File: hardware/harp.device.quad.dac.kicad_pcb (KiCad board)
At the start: 4 copper layers, 90 x 100 mm, 290 parts, among them J1 5-146281-3, J10 Conn_Coaxial, J11 Conn_Coaxial, J12 Conn_Coaxial, J13 Conn_Coaxial, J14 Barrel_Jack_Switch, J15 Conn_Coaxial, J16 Conn_Coaxial, J17 Conn_Coaxial, J18 Conn_Coaxial, J2 5-146281-3, J3 AudioJack3, J4 USB_C_Receptacle_USB2.0, J5 Micro_SD_Card_Det_Hirose_DM3AT, J6 Conn_Coaxial, J7 Conn_Coaxial, J8 Conn_Coaxial, J9 Conn_Coaxial, Q1 Si2369DS, Q2 Si2369DS, Q3 Si2369DS, SW2 SPST-NO, U1 LM337_SOT223, U10 LTC2642, U11 LTC2642, U12 REF3525, U13 LMV393IDGKR, U14 LMV393IDGKR, U15 LMV393IDGKR, U16 LMV393IDGKR, U17 INA630, U18 INA630, U19 INA630, U2 W25Q16JVUXIQ, U20 INA630, U21 REF2033, U22 SN74LVC2T45DCTR, U23 SN74LVC2T45DCTR, U24 rt6150b-33gqw, U25 TPS65131RGE, U27 LM2940IMPX-12/NOPB, U29 LMR51430, U3 ADUM4160, U30 SN74LVC2T45DCTR, U31 SN74LVC2T45DCTR, U32 RP2350_80QFN, U4 OPA2994IDGKR, U5 OPA2994IDGKR, U6 OPA2994IDGKR, U7 OPA2994IDGKR, U8 LTC2642, U9 LTC2642

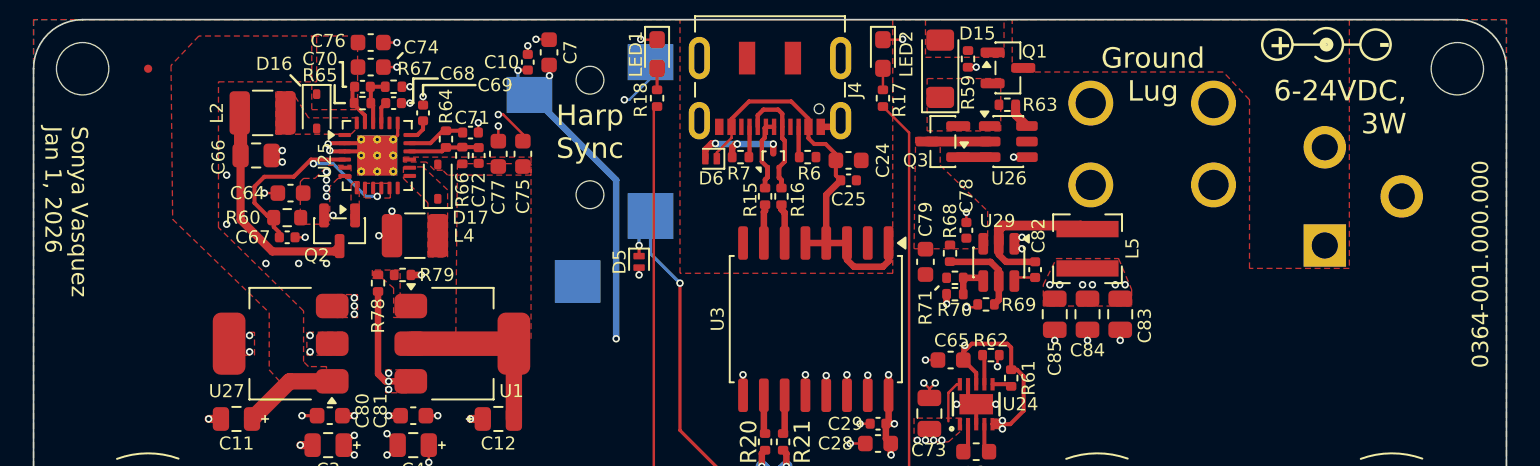
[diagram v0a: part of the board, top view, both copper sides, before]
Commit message: update 1K, 31K6, 10K resistors to 0.1%
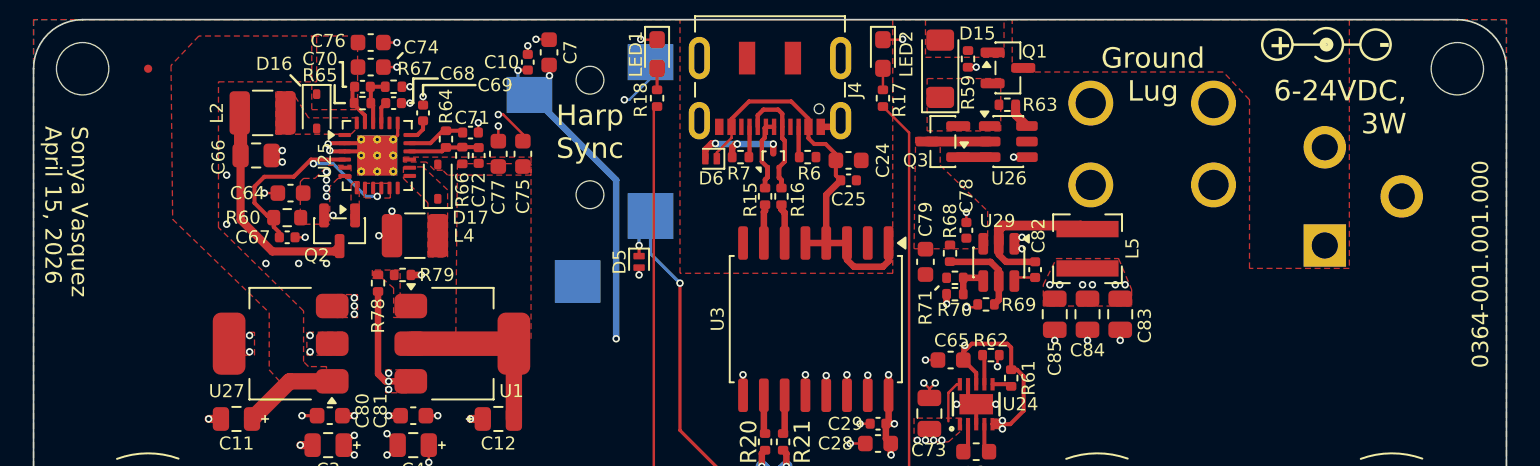
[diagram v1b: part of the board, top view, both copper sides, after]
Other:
- board text added: "0364-001.001.000"
- board text added: "Sonya Vasquez April 15, 2026"
- board text removed: "0364-001.000.000"
- board text removed: "Sonya Vasquez Jan 1, 2026"

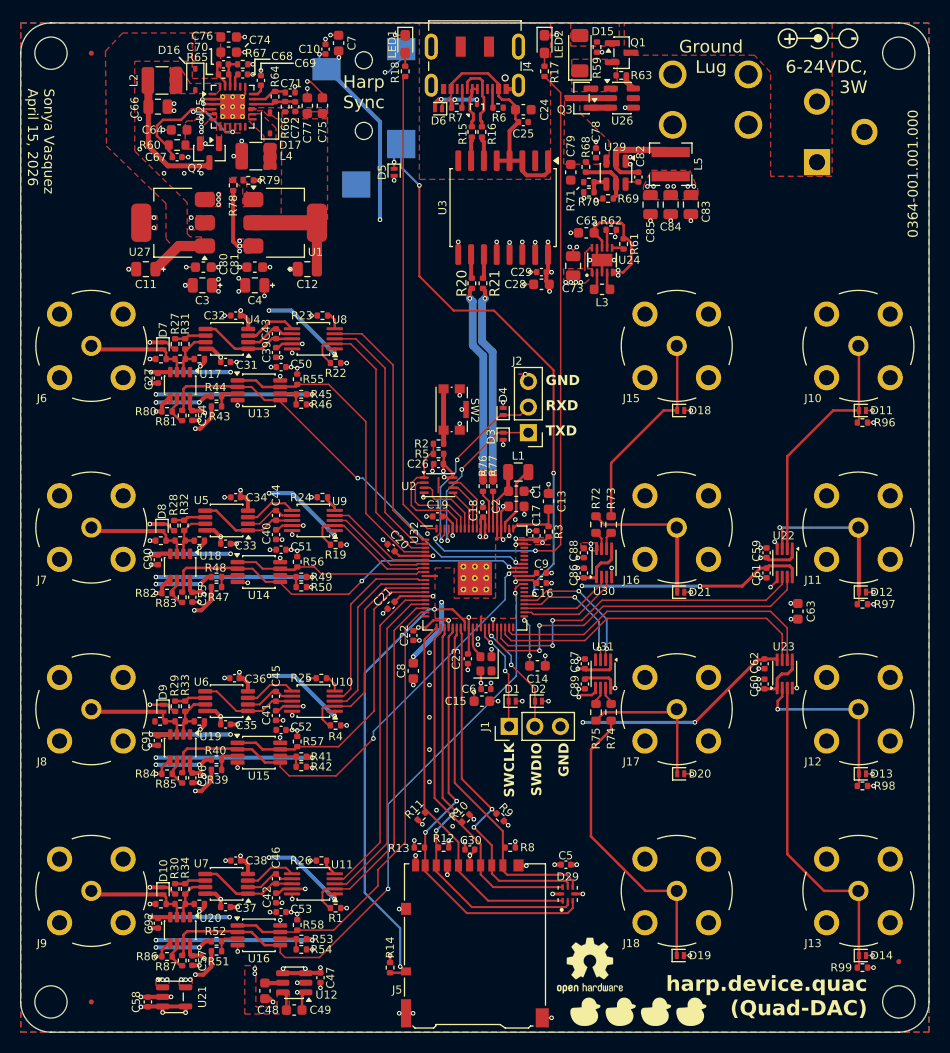
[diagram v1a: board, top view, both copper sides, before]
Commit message: swap BNC connectors to taller versions
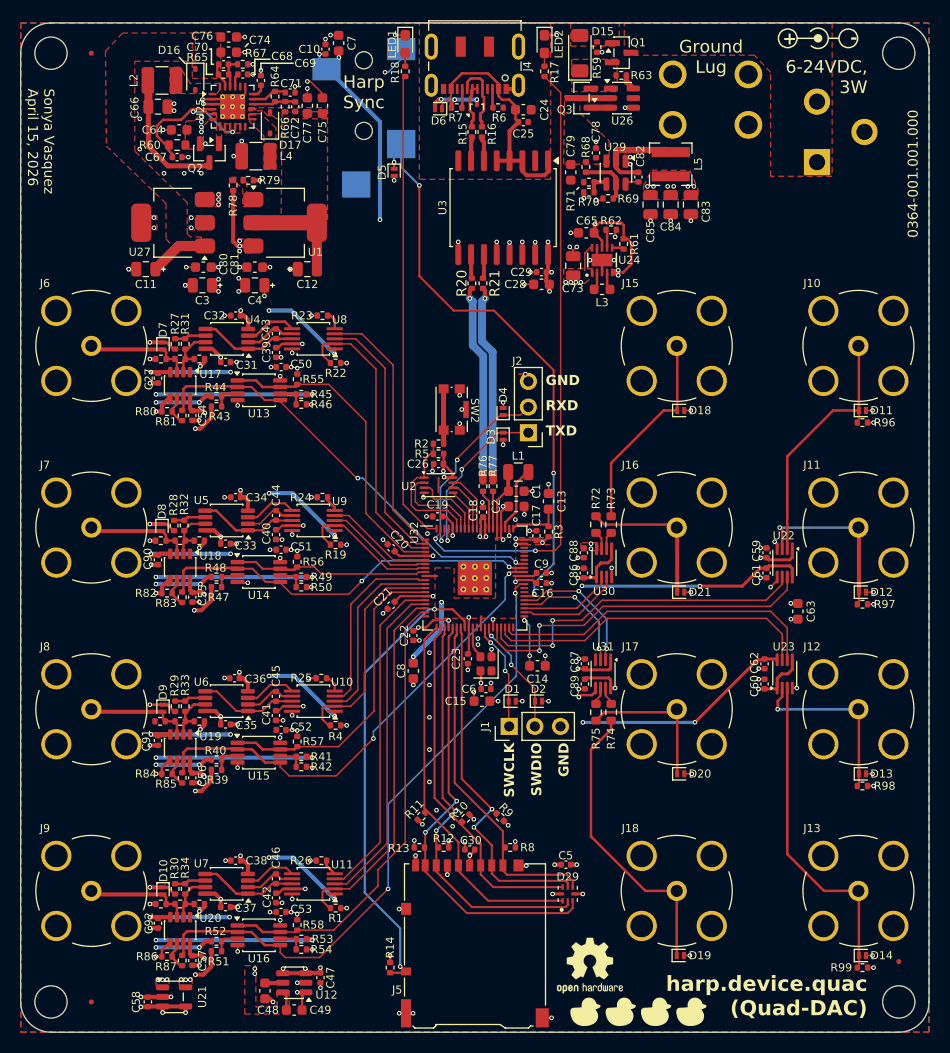
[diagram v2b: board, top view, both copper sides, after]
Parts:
- J10, J11, J12, J13, J15, J16, J17, J18, J6, J7, J8, J9: footprint kicad-lib:BNC_TEConnectivity_CONBNC001_Vertical -> kicad-lib:BNC_AmphenolRF_031-5329-52RFX_Vertical
